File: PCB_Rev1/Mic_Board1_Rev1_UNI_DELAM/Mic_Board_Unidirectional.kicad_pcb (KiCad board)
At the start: 2 copper layers, 51 x 31.5 mm, 30 parts, among them J1 Conn_01x03_Pin, J2 532610771, J3 S2B-ZR-SM4A-TF_LF__SN_, U1 OPA1671IDBVR

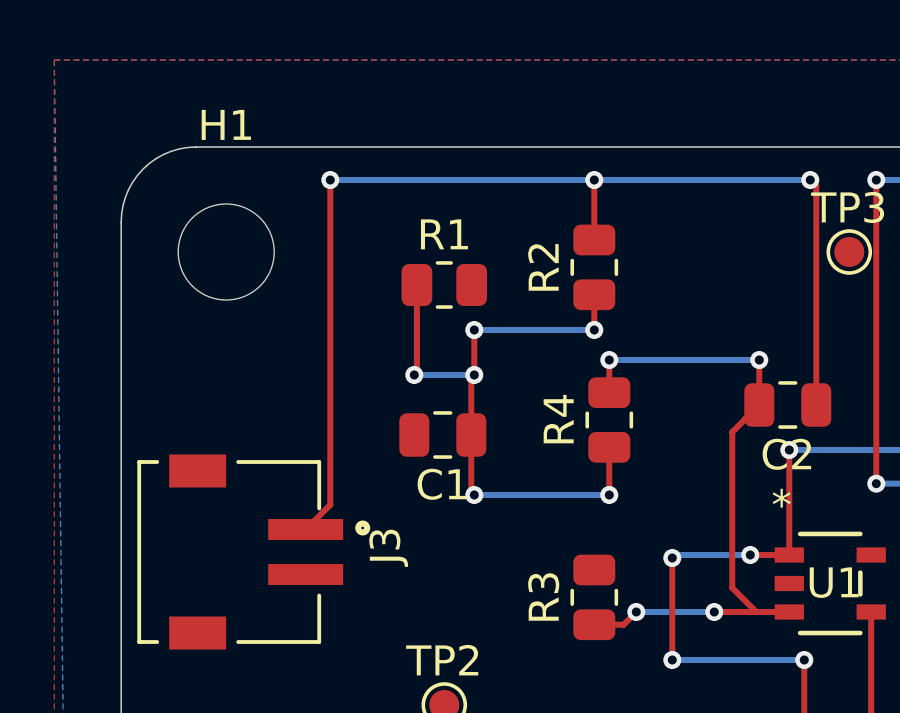
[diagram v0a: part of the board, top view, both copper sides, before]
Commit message: Ground Plane + Mic Board Adjustments
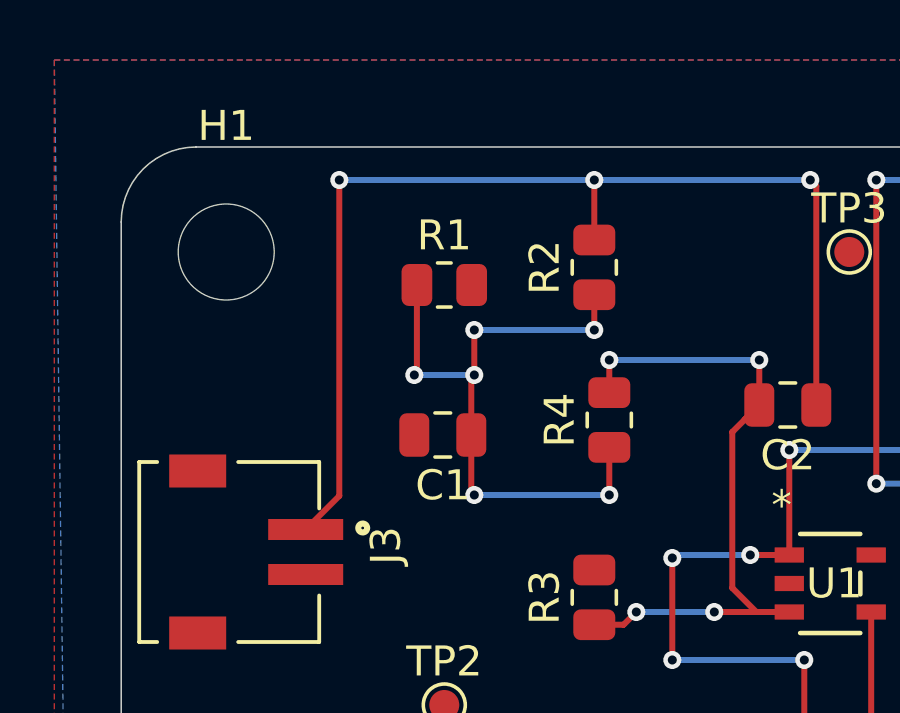
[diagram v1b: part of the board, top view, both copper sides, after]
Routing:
- added copper zone on In2.Cu, net GND
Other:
- copper layers 2 -> 4
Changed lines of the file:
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@@
 	(layers
 		(0 "F.Cu" signal)
+		(1 "In1.Cu" signal)
+		(2 "In2.Cu" signal)
 		(31 "B.Cu" signal)
 		(32 "B.Adhes" user "B.Adhesive")
@@
 			)
 			(layer "dielectric 1"
+				(type "prepreg")
+				(thickness 0.1)
+				(material "FR4")
+				(epsilon_r 4.5)
+				(loss_tangent 0.02)
+			)
+			(layer "In1.Cu"
+				(type "copper")
+				(thickness 0.035)
+			)
+			(layer "dielectric 2"
 				(type "core")
-				(thickness 1.51)
+				(thickness 1.24)
+				(material "FR4")
+				(epsilon_r 4.5)
+				(loss_tangent 0.02)
+			)
+			(layer "In2.Cu"
+				(type "copper")
+				(thickness 0.035)
+			)
+			(layer "dielectric 3"
+				(type "prepreg")
+				(thickness 0.1)
 				(material "FR4")
 				(epsilon_r 4.5)
@@
 	)
 	(segment
-		(start 135.2 77.830502)
-		(end 134.3805 78.650002)
+		(start 135.5 67)
+		(end 135.5 77.530502)
 		(width 0.2)
 		(layer "F.Cu")
@@
 	)
 	(segment
-		(start 135.2 67)
-		(end 135.2 77.830502)
+		(start 135.5 77.530502)
+		(end 134.3805 78.650002)
 		(width 0.2)
 		(layer "F.Cu")
@@
 	)
 	(via
-		(at 135.2 67)
+		(at 135.5 67)
 		(size 0.6)
 		(drill 0.3)
@@
 	)
 	(segment
-		(start 151.2 67)
+		(start 135.5 67)
 		(end 144 67)
 		(width 0.2)
@@
 	)
 	(segment
-		(start 135.2 67)
+		(start 151.2 67)
 		(end 144 67)
 		(width 0.2)
@@
 		(min_thickness 0.25)
 		(filled_areas_thickness no)
-		(fill
+		(fill yes
 			(thermal_gap 0.5)
 			(thermal_bridge_width 0.5)
@@
 		(net 2)
 		(net_name "GND")
+		(layer "In2.Cu")
+		(name "GND")
+		(hatch edge 0.5)
+		(priority 2)
+		(connect_pads
+			(clearance 0)
+		)
+		(min_thickness 0.25)
+		(filled_areas_thickness no)
+		(fill yes
+			(thermal_gap 0.5)
+			(thermal_bridge_width 0.5)
+		)
+		(polygon
+			(pts
+				(xy 128 65.5) (xy 179.5 65.5) (xy 179.5 98.5) (xy 127.5 98.5)
+			)
+		)
+	)
+	(zone
+		(net 2)
+		(net_name "GND")
 		(layer "B.Cu")
 		(name "PWR")
@@
 		(min_thickness 0.25)
 		(filled_areas_thickness no)
-		(fill
+		(fill yes
 			(thermal_gap 0.5)
 			(thermal_bridge_width 0.5)

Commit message: Routing
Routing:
- net Net-(U1-OUT): track 41.0 -> 51.1 mm
- net Net-(U1-+IN): track 23.7 -> 30.5 mm
- net Net-(U2-VCOM): track 24.6 -> 23.1 mm
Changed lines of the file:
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@@
+	)
+	(segment
+		(start 140 73.5)
+		(end 139.9 73.6)
+		(width 0.2)
+		(layer "F.Cu")
+		(net 1)
+	)
+	(segment
+		(start 139.9 75.5)
+		(end 139.9 77.4)
+		(width 0.2)
+		(layer "F.Cu")
+		(net 1)
+	)
+	(segment
+		(start 138.0875 70.5)
+		(end 138.0875 73.4125)
+		(width 0.2)
+		(layer "F.Cu")
+		(net 1)
+	)
+	(segment
+		(start 144.5 77.5)
+		(end 144.5 75.9125)
+		(width 0.2)
+		(layer "F.Cu")
+		(net 1)
+	)
+	(segment
+		(start 144 70.825)
+		(end 144 72)
+		(width 0.2)
+		(layer "F.Cu")
+		(net 1)
+	)
+	(segment
+		(start 139.9 73.6)
+		(end 139.9 75.5)
+		(width 0.2)
+		(layer "F.Cu")
+		(net 1)
 	)
 	(segment
@@
 	)
 	(segment
-		(start 139.9 73.6)
-		(end 139.9 75.5)
-		(width 0.2)
-		(layer "F.Cu")
-		(net 1)
-	)
-	(segment
-		(start 139.9 75.5)
-		(end 139.9 77.4)
-		(width 0.2)
-		(layer "F.Cu")
-		(net 1)
-	)
-	(segment
-		(start 138.0875 70.5)
-		(end 138.0875 73.4125)
-		(width 0.2)
-		(layer "F.Cu")
-		(net 1)
-	)
-	(segment
-		(start 144.5 77.5)
-		(end 144.5 75.9125)
-		(width 0.2)
-		(layer "F.Cu")
-		(net 1)
-	)
-	(segment
-		(start 144 70.825)
-		(end 144 72)
-		(width 0.2)
-		(layer "F.Cu")
-		(net 1)
-	)
-	(segment
-		(start 140 73.5)
-		(end 139.9 73.6)
-		(width 0.2)
-		(layer "F.Cu")
-		(net 1)
-	)
-	(segment
 		(start 138.0875 73.4125)
 		(end 138 73.5)
@@
 	)
 	(segment
+		(start 140 77.5)
+		(end 144.5 77.5)
+		(width 0.2)
+		(layer "B.Cu")
+		(net 1)
+	)
+	(segment
+		(start 140 72)
+		(end 144 72)
+		(width 0.2)
+		(layer "B.Cu")
+		(net 1)
+	)
+	(segment
 		(start 138 73.5)
 		(end 140 73.5)
@@
 	)
 	(segment
-		(start 140 77.5)
-		(end 144.5 77.5)
-		(width 0.2)
-		(layer "B.Cu")
-		(net 1)
-	)
-	(segment
-		(start 140 72)
-		(end 144 72)
-		(width 0.2)
-		(layer "B.Cu")
-		(net 1)
-	)
-	(segment
 		(start 149.5 74.5)
 		(end 149.000062 74.999938)
@@
 	)
 	(segment
+		(start 139 84.5)
+		(end 142.5 84.5)
+		(width 0.2)
+		(layer "F.Cu")
+		(net 3)
+	)
+	(segment
 		(start 149.5 73)
 		(end 149.5 74.5)
@@
 	)
 	(segment
+		(start 142.5 84.5)
+		(end 144 83)
+		(width 0.2)
+		(layer "F.Cu")
+		(net 3)
+	)
+	(segment
 		(start 144.5 74.0875)
 		(end 144.5 73)
@@
 	)
 	(segment
+		(start 144 83)
+		(end 144 81.825)
+		(width 0.2)
+		(layer "F.Cu")
+		(net 3)
+	)
+	(segment
 		(start 149.5 74.5)
 		(end 148.6 75.4)
@@
 	)
 	(segment
+		(start 147.2305 93.0305)
+		(end 148.2 94)
+		(width 0.2)
+		(layer "F.Cu")
+		(net 6)
+	)
+	(segment
+		(start 152.5 75.7)
+		(end 150.5 77.7)
+		(width 0.2)
+		(layer "F.Cu")
+		(net 6)
+	)
+	(segment
 		(start 150.5 79.5)
 		(end 149.2 79.5)
@@
 	)
 	(segment
-		(start 149.400002 94.5)
-		(end 150 93.900002)
-		(width 0.2)
-		(layer "F.Cu")
-		(net 6)
-	)
-	(segment
-		(start 148 94.5)
-		(end 149.400002 94.5)
+		(start 148.2 94)
+		(end 149.900002 94)
 		(width 0.2)
 		(layer "F.Cu")
@@
 	)
 	(segment
-		(start 147.2305 93.7305)
-		(end 148 94.5)
-		(width 0.2)
-		(layer "F.Cu")
-		(net 6)
-	)
-	(segment
 		(start 147.2305 88.725002)
-		(end 147.2305 93.7305)
+		(end 147.2305 93.0305)
+		(width 0.2)
+		(layer "F.Cu")
+		(net 6)
+	)
+	(segment
+		(start 150.5 77.7)
+		(end 150.5 79.5)
+		(width 0.2)
+		(layer "F.Cu")
+		(net 6)
+	)
+	(segment
+		(start 149.900002 94)
+		(end 150 93.900002)
 		(width 0.2)
 		(layer "F.Cu")
@@
 		(net 6)
 	)
+	(segment
+		(start 152.5 69.400002)
+		(end 152.5 75.7)
+		(width 0.2)
+		(layer "F.Cu")
+		(net 6)
+	)
 	(via
 		(at 146.6 79.6)
@@
 	)
 	(segment
-		(start 157.2805 67.2805)
+		(start 154.2 67)
+		(end 154.2 77.12225)
+		(width 0.2)
+		(layer "F.Cu")
+		(net 12)
+	)
+	(segment
+		(start 157.2805 67.0805)
 		(end 157.2805 69.900002)
 		(width 0.2)
@@
 	)
 	(segment
-		(start 157 67)
-		(end 157.2805 67.2805)
+		(start 157.2 67)
+		(end 157.2805 67.0805)
 		(width 0.2)
 		(layer "F.Cu")
 		(net 12)
 	)
-	(segment
-		(start 153.4 77.12225)
-		(end 153.4 67)
-		(width 0.2)
-		(layer "F.Cu")
+	(via
+		(at 154.2 67)
+		(size 0.6)
+		(drill 0.3)
+		(layers "F.Cu" "B.Cu")
 		(net 12)
 	)
 	(via
-		(at 153.4 67)
+		(at 158.77775 77.12225)
 		(size 0.6)
 		(drill 0.3)
@@
 	)
 	(via
-		(at 158.77775 77.12225)
+		(at 154.2 77.12225)
 		(size 0.6)
 		(drill 0.3)
@@
 	)
 	(via
-		(at 153.4 77.12225)
+		(at 157.2 67)
 		(size 0.6)
 		(drill 0.3)
@@
 		(net 12)
 	)
-	(via
-		(at 157 67)
-		(size 0.6)
-		(drill 0.3)
-		(layers "F.Cu" "B.Cu")
+	(segment
+		(start 154.2 77.12225)
+		(end 158.77775 77.12225)
+		(width 0.2)
+		(layer "B.Cu")
 		(net 12)
 	)
 	(segment
-		(start 153.4 67)
-		(end 157 67)
-		(width 0.2)
-		(layer "B.Cu")
-		(net 12)
-	)
-	(segment
-		(start 153.4 77.12225)
-		(end 158.77775 77.12225)
+		(start 154.2 67)
+		(end 157.2 67)
 		(width 0.2)
 		(layer "B.Cu")
@@
 	)
 	(segment
-		(start 169.5 84.5)
-		(end 169.175001 84.175001)
+		(start 170.175001 84.175001)
+		(end 164.68325 84.175001)
+		(width 0.2)
+		(layer "F.Cu")
+		(net 18)
+	)
+	(segment
+		(start 171.225001 85.225001)
+		(end 170.175001 84.175001)
 		(width 0.2)
 		(layer "F.Cu")
@@
 	)
 	(segment
-		(start 171.225001 85.225001)
-		(end 170.5 84.5)
-		(width 0.2)
-		(layer "F.Cu")
-		(net 18)
-	)
-	(segment
-		(start 169.175001 84.175001)
-		(end 164.68325 84.175001)
-		(width 0.2)
-		(layer "F.Cu")
-		(net 18)
-	)
-	(segment
-		(start 170.5 84.5)
-		(end 169.5 84.5)
-		(width 0.2)
-		(layer "F.Cu")
-		(net 18)
-	)
-	(segment
 		(start 171 84)
 		(end 171.024999 83.975001)
@@
 	)
 	(segment
-		(start 170.524997 82.225003)
-		(end 171.274999 81.475001)
+		(start 170.774997 82.225003)
+		(end 171.524999 81.475001)
 		(width 0.2)
 		(layer "F.Cu")
@@
 	(segment
 		(start 164.68325 82.225003)
-		(end 170.524997 82.225003)
+		(end 170.774997 82.225003)
 		(width 0.2)
 		(layer "F.Cu")
@@
 	)
 	(segment
-		(start 171.274999 81.475001)
+		(start 171.524999 81.475001)
 		(end 172.736 81.475001)
 		(width 0.2)
@@
 		(min_thickness 0.25)
 		(filled_areas_thickness no)
-		(fill yes
+		(fill
 			(thermal_gap 0.5)
 			(thermal_bridge_width 0.5)
@@
 		(min_thickness 0.25)
 		(filled_areas_thickness no)
-		(fill yes
+		(fill
 			(thermal_gap 0.5)
 			(thermal_bridge_width 0.5)
@@
 		(min_thickness 0.25)
 		(filled_areas_thickness no)
-		(fill yes
+		(fill
 			(thermal_gap 0.5)
 			(thermal_bridge_width 0.5)

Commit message: Uni Delam Rev 1 Complete ?
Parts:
- moved C6 1.72 mm to (153.6, 89.5), turned to 0 degrees
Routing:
- net GND: track 0.00 -> 144.3 mm, vias 0 -> 16
- net +3V3: track 0.00 -> 68.0 mm, vias 0 -> 15
- net Net-(U1-OUT): track 51.1 -> 47.6 mm, vias 8 -> 9
- net Net-(U2-VCOM): track 23.1 -> 24.6 mm
- net Net-(U2-MCLK): track 8.11 -> 8.72 mm, vias 0 -> 2
- net Net-(C2-Pad1): track 37.4 -> 36.8 mm
- net Net-(U1-+IN): track 30.5 -> 31.1 mm
- net Net-(U2-LRCK): track 8.26 -> 8.59 mm, vias 0 -> 2
- net Net-(U2-SDTO): track 8.49 -> 8.79 mm, vias 0 -> 2
- net Net-(U2-BICK): track 8.36 -> 8.44 mm, vias 0 -> 2
- removed copper zone on F.Cu, net +3V3
- removed copper zone on B.Cu, net GND
- removed copper zone on In2.Cu, net GND
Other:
- copper layers 4 -> 2
